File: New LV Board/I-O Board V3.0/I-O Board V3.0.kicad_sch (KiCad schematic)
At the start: 19 parts, among them J1 PH1-10-UA, J10 691137710002, J11 691137710002, J13 691137710002, J2 *, J3 *, J4 *, J5 Conn_01x15, J6 Conn_01x15, J7 Conn_01x15, J8 691137710002, J9 691137710002

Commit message: IO Board V3.0 done?
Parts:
- removed J10, J11, J13, J8, J9: 691137710002, I-O_Footprints:691137710002, symbol 691137710002:691137710002
- added J16, J17, J18, J19, J20: 2604-1101, MotorSports_KICad:CONN_2604-1101_WAG, symbol 2025-11-13_21-26-34:2604-1101
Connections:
- net at J1.1, J1.2, J1.3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: now also J18.1 (1_1), J18.2 (1_2), J19.1 (1_1), J19.2 (1_2)
- net at F1.1, F1.2: now also J16.1 (1_1), J16.2 (1_2), J20.1 (1_1), J20.2 (1_2)
- net at F1.3, F1.4: now also J17.1 (1_1), J17.2 (1_2)
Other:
- note added: "GLV + bus bar (decrepit)"
- note added: "GLV TO VCU VBATT (decrepiot, 3 wires)"
- note added: "GLV out to car"
- note added: "GLV- bus bar (decrepit)"
- note added: "GLV- whole car"
- note added: "Removed"
- note added: "Robin Sean Board -"
- note added: "Robin and Sean Board +"
- note added: "V-Bat"
- note removed: "IMD Reset +"
- moved on the sheet: F1

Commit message: now IO should be done (fingers crossed)
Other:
- note added: "GLV +"
- note added: "VCU GLV +"
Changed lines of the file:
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@@
 		)
 	)
-	(text "Unused"
-		(exclude_from_sim no)
-		(at 147.066 88.138 0)
+`	(text "VCU GLV +"
+		(exclude_from_sim no)
+		(at 147.066 85.598 0)
 		(effects
 			(font
@@
 		)
 	)
+	(text "GLV +"
+		(exclude_from_sim no)
+		(at 147.066 92.964 0)
+		(effects
+			(font
+				(size 1.27 1.27)
+			)
+		)
+	)
 	(text "Unused"
 		(exclude_from_sim no)
@@
 		)
 	)
-	(text "Unused"
-		(exclude_from_sim no)
-		(at 147.066 95.758 0)
-		(effects
-			(font
-				(size 1.27 1.27)
-			)
-		)
-	)
 	(text "VCU Charge Enable (5V)"
 		(exclude_from_sim no)
@@
 		)
 	)
-	(text "Unused"
-		(exclude_from_sim no)
-		(at 147.066 93.218 0)
+	(text "VCU GLV +"
+		(exclude_from_sim no)
+		(at 146.9291 88.138 0)
 		(effects
 			(font
@@
 		)
 	)
-	(text "Unused"
+	(text "GLV +"
 		(exclude_from_sim no)
 		(at 147.066 90.678 0)
@@
 		)
 	)
+	(text "GLV +"
+		(exclude_from_sim no)
+		(at 147.066 95.504 0)
+		(effects
+			(font
+				(size 1.27 1.27)
+			)
+		)
+	)
 	(text "From Charge Enable Switch"
 		(exclude_from_sim no)
@@
 		)
 	)
-	(text "Unused"
+	(text "VCU GLV +"
 		(exclude_from_sim no)
 		(at 147.066 83.058 0)
@@
 			)
 		)
-	)
-	(text "Unused"
-		(exclude_from_sim no)
-		(at 147.066 85.598 0)
-		(effects
-			(font
-				(size 1.27 1.27)
-			)
-		)

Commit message: Revert "now IO should be done (fingers crossed)"
This reverts commit 0e71786429b188e83ce6d05af818c70c1a18e264.
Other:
- note removed: "GLV +"
- note removed: "VCU GLV +"

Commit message: IO Board changes
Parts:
- removed J1: PH1-10-UA, MotorSports_KICad:HDRV10W64P0X254_1X10_2540X249X886P, symbol PH1-10-UA:PH1-10-UA
- added J8: 2604-1101, I-O_Footprints:CONN_2604-1101_WAG, symbol 2025-11-13_21-26-34:2604-1101
- J4: renamed from J20; footprint MotorSports_KICad:CONN_2604-1101_WAG -> I-O_Footprints:CONN_2604-1101_WAG
- J5: renamed from J19; footprint MotorSports_KICad:CONN_2604-1101_WAG -> I-O_Footprints:CONN_2604-1101_WAG
- J6: renamed from J16; footprint MotorSports_KICad:CONN_2604-1101_WAG -> I-O_Footprints:CONN_2604-1101_WAG
- J7: renamed from J18; footprint MotorSports_KICad:CONN_2604-1101_WAG -> I-O_Footprints:CONN_2604-1101_WAG
- J9: renamed from J17; footprint MotorSports_KICad:CONN_2604-1101_WAG -> I-O_Footprints:CONN_2604-1101_WAG
- renumbered J2 to J1-A1, J5 to J1-B1, J3 to J2-A1, J6 to J2-B1, J4 to J3-A1, J7 to J3-B1, R26 to R1, R23 to R2, R29 to R3, R28 to R4, R30 to R5, R31 to R6
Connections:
- net at J3-B1.10 (Pin_10): now also J3-B1.8 (Pin_8), J3-B1.9 (Pin_9), J8.1 (1_1), J8.2 (1_2)
- net at J3-B1.11 (Pin_11): now also F1.1, F1.2, J3-B1.12 (Pin_12), J3-B1.13 (Pin_13), J4.1 (1_1), J4.2 (1_2), J6.1 (1_1), J6.2 (1_2)
- net at J3-B1.14 (Pin_14): now also J1-A1.S1 (SHIELD), J1-A1.S2 (SHIELD), J2-A1.S1 (SHIELD), J2-A1.S2 (SHIELD), J3-A1.S1 (SHIELD), J3-A1.S2 (SHIELD), J3-B1.15 (Pin_15), J5.1 (1_1), J5.2 (1_2), J7.1 (1_1), J7.2 (1_2)
- no-connect marks 7 -> 0
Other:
- note added: "From Precharge Circuit"
- note added: "GLV+ 1"
- note added: "GLV+ 2"
- note added: "GLV+ 3"
- note added: "GLV- 1"
- note added: "GLV- 2"
- note added: "Hall Effect Sensor In"
- note added: "Hall Effect Sensor Out"
- note added: "Throttle Analog Signal to MC J1-13 (Unused)"
- note added: "Throttle PWM from VCU Output 7 (Unused)"
- note added: "VCU GLV 1"
- note added: "VCU GLV 2"
- note added: "VCU GLV 3"
- note added: "VCU GLV+"
- note removed: "Precharge Coil -"
- moved on the sheet: R3, R4, R6

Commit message: pin switcheroo
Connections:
- net at J3-B1.1 (Pin_1): now also J3-B1.10 (Pin_10), J3-B1.9 (Pin_9), J8.1 (1_1), J8.2 (1_2); no longer J3-A1.02
- net at J3-B1.2 (Pin_2): now also J3-A1.02; no longer R1.2
- net at J3-B1.4 (Pin_4): now also R1.2; no longer J3-A1.05
- net at J3-B1.5 (Pin_5): now also J3-A1.05; no longer J3-A1.06
- net at J3-B1.6 (Pin_6): now also J3-A1.06; no longer J3-A1.07
- net at J3-B1.7 (Pin_7): now also J3-A1.07; no longer R2.2
- new net: J3-B1.8 (Pin_8), R2.2
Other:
- note removed: "TSMS Vs"

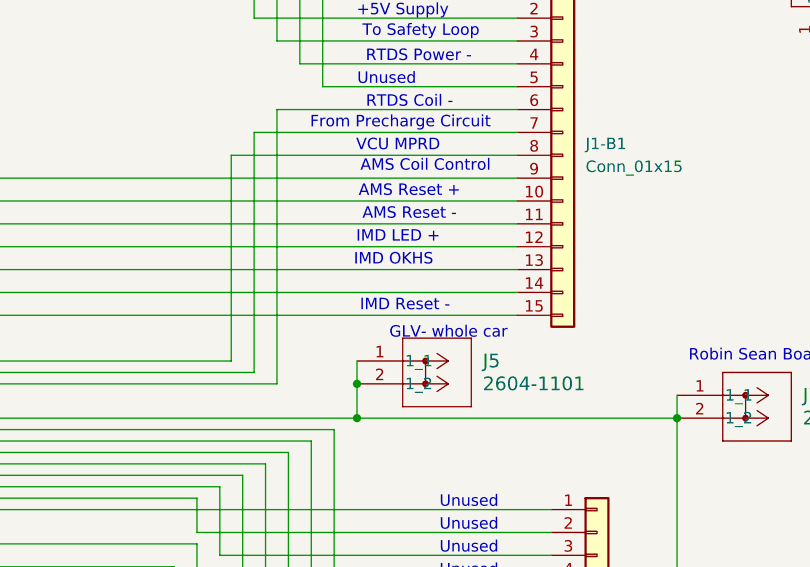
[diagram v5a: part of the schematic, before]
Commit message: Changed file name of VCU Throttle Latching to Throttle Latching Module, attempt to make VCU MPR & IMD Latch into IMD Latch & AMS Latch.
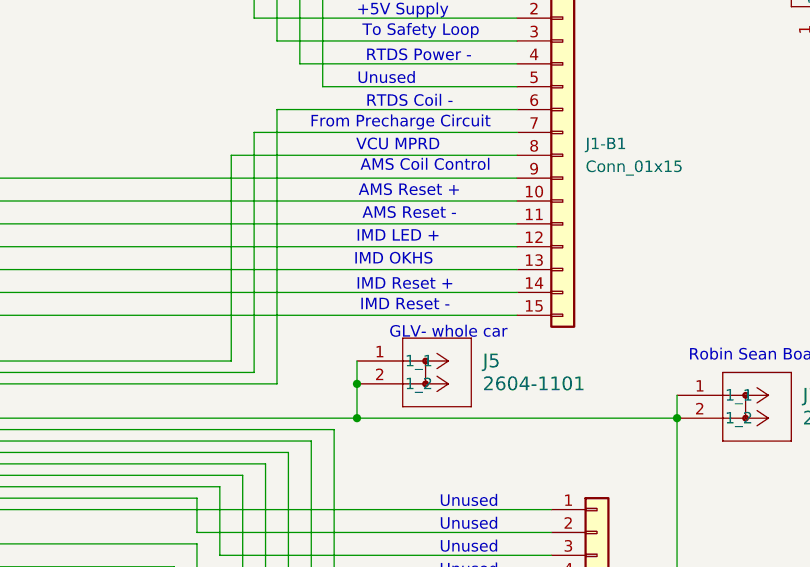
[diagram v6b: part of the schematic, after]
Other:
- note added: "IMD Reset +"
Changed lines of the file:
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@@
+		)
+	)
+	(text "IMD Reset +"
+		(exclude_from_sim no)
+		(at 139.954 58.928 0)
+		(effects
+			(font
+				(size 1.27 1.27)
+			)
 		)
 	)

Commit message: traces probably
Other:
- note added: "Hall Effect Vref In"
- note added: "RTDS VCU"
- note added: "Reserved Input 1"
- note added: "Reserved Input 2"
- note added: "Reserved Input 3"
- note added: "Reserved Input 4"
- note removed: "RTDS Power -"
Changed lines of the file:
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@@
+		)
+	)
+	(text "Reserved Input 2"
+		(exclude_from_sim no)
+		(at 142.748 105.918 0)
+		(effects
+			(font
+				(size 1.27 1.27)
+			)
 		)
 	)
@@
 		)
 	)
-	(text "Unused"
-		(exclude_from_sim no)
-		(at 147.066 108.458 0)
-		(effects
-			(font
-				(size 1.27 1.27)
-			)
-		)
-	)
 	(text "IMD Reset +"
 		(exclude_from_sim no)
@@
 		)
 	)
+	(text "Reserved Input 1"
+		(exclude_from_sim no)
+		(at 142.748 108.458 0)
+		(effects
+			(font
+				(size 1.27 1.27)
+			)
+		)
+	)
 	(text "GLV+ 2"
 		(exclude_from_sim no)
@@
 		)
 	)
-	(text "Unused"
-		(exclude_from_sim no)
-		(at 147.066 103.378 0)
-		(effects
-			(font
-				(size 1.27 1.27)
-			)
-		)
-	)
 	(text "Hall Effect Sensor Out"
 		(exclude_from_sim no)
@@
 		)
 	)
-	(text "Unused"
-		(exclude_from_sim no)
-		(at 137.922 36.068 0)
+	(text "Hall Effect Vref In\n"
+		(exclude_from_sim no)
+		(at 143.51 36.068 0)
 		(effects
 			(font
@@
 		)
 	)
-	(text "Unused"
-		(exclude_from_sim no)
-		(at 147.066 105.918 0)
-		(effects
-			(font
-				(size 1.27 1.27)
-			)
-		)
-	)
 	(text "Robin and Sean Board +"
 		(exclude_from_sim no)
@@
 		)
 	)
-	(text "Unused"
-		(exclude_from_sim no)
-		(at 147.066 100.838 0)
-		(effects
-			(font
-				(size 1.27 1.27)
-			)
-		)
-	)
 	(text "Throttle PWM from VCU Output 7 (Unused) "
 		(exclude_from_sim no)
@@
 		)
 	)
+	(text "Reserved Input 3"
+		(exclude_from_sim no)
+		(at 142.748 103.378 0)
+		(effects
+			(font
+				(size 1.27 1.27)
+			)
+		)
+	)
 	(text "Unused"
 		(exclude_from_sim no)
@@
 		)
 	)
+	(text "Reserved Input 4"
+		(exclude_from_sim no)
+		(at 142.748 100.584 0)
+		(effects
+			(font
+				(size 1.27 1.27)
+			)
+		)
+	)
 	(text "AMS Reset -"
 		(exclude_from_sim no)
@@
 		)
 	)
-	(text "RTDS Power -"
-		(exclude_from_sim no)
-		(at 141.478 33.528 0)
-		(effects
-			(font
+	(text "RTDS VCU"
+		(exclude_from_sim no)
+		(at 139.446 33.274 0)
+		(effects
+			(font

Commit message: BANG
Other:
- note added: "From Precharge"
- note added: "GLV+"
- note added: "GLV-"
- note added: "Temp sensor pull up"
- note added: "VBatt (Vehicle Battery from GLVMS before 20A fuse)"
- note removed: "From Precharge Circuit"
- note removed: "GLV+ 1"
- note removed: "GLV+ 2"
- note removed: "GLV+ 3"
- note removed: "GLV- 1"
- note removed: "GLV- 2"
- note removed: "V-Bat"
- note removed: "VCU GLV 1"
- note removed: "VCU GLV 2"
- note removed: "VCU GLV 3"
- note removed: "Vs"
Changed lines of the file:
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@@
 	(generator_version "9.0")
 	(paper "A4")
-	(text "V-Bat"
+	(text "VBatt (Vehicle Battery from GLVMS before 20A fuse)"
 		(exclude_from_sim no)
 		(at 186.69 18.542 0)
@@
 		)
 	)
-	(text "VCU GLV 2"
+	(text "VCU GLV+"
 		(exclude_from_sim no)
 		(at 146.304 152.908 0)
@@
 		)
 	)
-	(text "GLV+ 3"
+	(text "GLV+"
 		(exclude_from_sim no)
 		(at 147.828 163.068 0)
@@
 		)
 	)
-	(text "GLV+ 2"
+	(text "GLV+"
 		(exclude_from_sim no)
 		(at 147.828 160.528 0)
@@
 		)
 	)
-	(text "GLV- 1"
+	(text "GLV-"
 		(exclude_from_sim no)
 		(at 148.082 165.354 0)
@@
 		)
 	)
-	(text "GLV- 2"
+	(text "GLV-"
 		(exclude_from_sim no)
 		(at 148.082 168.402 0)
@@
 		)
 	)
-	(text "VCU GLV 1"
+	(text "VCU GLV+"
 		(exclude_from_sim no)
 		(at 147.066 132.334 0)
@@
 		)
 	)
-	(text "VCU GLV 3"
+	(text "VCU GLV+"
 		(exclude_from_sim no)
 		(at 146.304 155.448 0)
@@
 		)
 	)
-	(text "From Precharge Circuit"
+	(text "From Precharge"
 		(exclude_from_sim no)
 		(at 139.446 40.894 0)
@@
 		)
 	)
-	(text "Vs"
+	(text "Temp sensor pull up"
 		(exclude_from_sim no)
 		(at 133.35 139.954 0)
@@
 		)
 	)
-	(text "GLV+ 1"
+	(text "GLV+"
 		(exclude_from_sim no)
 		(at 147.828 157.734 0)
